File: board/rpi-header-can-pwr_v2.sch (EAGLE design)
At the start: 41 parts, among them U1 MCP2515, X1 RJ45-8L21-S, X2 RASPI_BOARD_B+#_E3

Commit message: add board temp sensor add battery voltage sensor
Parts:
- added C13, C15: 100n, rcl:C-EUC0603
- added C14: 1u, rcl:C-EUC0603
- added R7: 0, resistor:R-EU_R0603
- added R8, R9: 4.7K, resistor:R-EU_R0603
- added U2: ADS1015, SparkFun-IC-Conversion:ADS1015
- added U3: BME280, SparkFun-Sensors:BME280
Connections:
- new net ADC_ALERT: R7.1, X2.GPIO21
- new net ADC_INPUT_1: U2.AIN0
- new net I2C_SCL: R9.2, U2.SCL, U3.SCK/SCL, X2.SCL
- new net I2C_SDA: R8.2, U2.SDA, U3.SDI/SDA, X2.SDA
- new net N$9: R7.2, U2.ALERT/RDY
- net +3V3: now also C13.1, C14.1, C15.1, R8.1, R9.1, U2.VDD, U3.!CS, U3.VDD, U3.VDDIO
- net GND: now also C13.2, C14.2, C15.2, U2.ADDR, U2.VSS, U3.GND, U3.SDO/ADR

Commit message: ADC ALERT requires pull up
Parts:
- added R10: 4.7K, resistor:R-EU_R0603
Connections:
- net +3V3: now also R10.2
- net N$9: now also R10.1
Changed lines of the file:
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@@
 <part name="C14" library="rcl" deviceset="C-EU" device="C0603" value="1u"/>
 <part name="C15" library="rcl" deviceset="C-EU" device="C0603" value="100n"/>
+<part name="R10" library="resistor" deviceset="R-EU_" device="R0603" value="4.7K"/>
+<part name="+3V10" library="supply1" deviceset="+3V3" device=""/>
 </parts>
 <sheets>
@@
 <instance part="GND22" gate="1" x="142.24" y="10.16" rot="R90"/>
 <instance part="+3V9" gate="G$1" x="142.24" y="22.86" rot="R270"/>
+<instance part="R10" gate="G$1" x="35.56" y="-12.7" rot="R90"/>
+<instance part="+3V10" gate="G$1" x="35.56" y="0"/>
 </instances>
 <busses>
@@
 <wire x1="139.7" y1="22.86" x2="134.62" y2="22.86" width="0.1524" layer="91"/>
 </segment>
+<segment>
+<pinref part="R10" gate="G$1" pin="2"/>
+<pinref part="+3V10" gate="G$1" pin="+3V3"/>
+<wire x1="35.56" y1="-2.54" x2="35.56" y2="-7.62" width="0.1524" layer="91"/>
+</segment>
 </net>
 <net name="CAN_H" class="0">
@@
 <pinref part="U2" gate="G$1" pin="ALERT/RDY"/>
 <pinref part="R7" gate="G$1" pin="2"/>
-<wire x1="40.64" y1="-22.86" x2="33.02" y2="-22.86" width="0.1524" layer="91"/>
-</segment>
-</net>
+<wire x1="40.64" y1="-22.86" x2="35.56" y2="-22.86" width="0.1524" layer="91"/>
+<pinref part="R10" gate="G$1" pin="1"/>
+<wire x1="35.56" y1="-22.86" x2="33.02" y2="-22.86" width="0.1524" layer="91"/>
+<wire x1="35.56" y1="-17.78" x2="35.56" y2="-22.86" width="0.1524" layer="91"/>
+<junction x="35.56" y="-22.86"/>
+</segment>
+</net>

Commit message: add voltage divider and gpio protection to battery voltage sensor
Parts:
- added C29: 10nF, eagle-ltspice:CC0603
- added D7: BAS70-04, diode:BAS70-04
- added R20: 68k, rcl:R-EU_R0603
- added R21: 20k, rcl:R-EU_R0603
- added R22: 1k, rcl:R-EU_R0603
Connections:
- new net 12V_REFERENCE4: D7.C1A2, R20.2, R21.2, R22.1
- net +12V: now also R20.1
- net +3V3: now also D7.C2
- net ADC_INPUT_1: now also C29.2, R22.2
- net GND: now also C29.1, D7.A1, R21.1
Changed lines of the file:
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@@
 <part name="GND19" library="supply1" deviceset="GND" device=""/>
 <part name="R7" library="resistor" deviceset="R-EU_" device="R0603" value="0"/>
-<part name="P+8" library="supply1" deviceset="+12V" device=""/>
 <part name="R8" library="resistor" deviceset="R-EU_" device="R0603" value="4.7K"/>
 <part name="R9" library="resistor" deviceset="R-EU_" device="R0603" value="4.7K"/>
@@
 <part name="R10" library="resistor" deviceset="R-EU_" device="R0603" value="4.7K"/>
 <part name="+3V10" library="supply1" deviceset="+3V3" device=""/>
+<part name="R20" library="rcl" deviceset="R-EU_" device="R0603" value="68k"/>
+<part name="R21" library="rcl" deviceset="R-EU_" device="R0603" value="20k"/>
+<part name="D7" library="diode" deviceset="BAS70-04" device=""/>
+<part name="+3V16" library="supply1" deviceset="+3V3" device=""/>
+<part name="GND48" library="supply1" deviceset="GND" device=""/>
+<part name="C29" library="eagle-ltspice" deviceset="C" device="C0603" value="10nF"/>
+<part name="GND49" library="supply1" deviceset="GND" device=""/>
+<part name="GND50" library="supply1" deviceset="GND" device=""/>
+<part name="R22" library="rcl" deviceset="R-EU_" device="R0603" value="1k"/>
+<part name="P+10" library="supply1" deviceset="+12V" device=""/>
 </parts>
 <sheets>
@@
 <instance part="GND19" gate="1" x="38.1" y="-30.48" rot="R90"/>
 <instance part="R7" gate="G$1" x="45.72" y="-22.86" rot="R180"/>
-<instance part="P+8" gate="1" x="-35.56" y="-68.58" rot="R90"/>
 <instance part="R8" gate="G$1" x="27.94" y="-60.96" rot="R180"/>
 <instance part="R9" gate="G$1" x="27.94" y="-68.58" rot="R180"/>
@@
 <instance part="R10" gate="G$1" x="35.56" y="-12.7" rot="R90"/>
 <instance part="+3V10" gate="G$1" x="35.56" y="0"/>
+<instance part="R20" gate="G$1" x="-76.2" y="-88.9"/>
+<instance part="R21" gate="G$1" x="-55.88" y="-93.98"/>
+<instance part="D7" gate="G$1" x="-50.8" y="-81.28" rot="R180"/>
+<instance part="+3V16" gate="G$1" x="-63.5" y="-81.28" rot="R90"/>
+<instance part="GND48" gate="1" x="-40.64" y="-81.28" rot="R90"/>
+<instance part="C29" gate="G$1" x="-35.56" y="-83.82"/>
+<instance part="GND49" gate="1" x="-35.56" y="-78.74" rot="R180"/>
+<instance part="GND50" gate="1" x="-66.04" y="-93.98" rot="R270"/>
+<instance part="R22" gate="G$1" x="-43.18" y="-88.9"/>
+<instance part="P+10" gate="1" x="-88.9" y="-88.9" rot="R90"/>
 </instances>
 <busses>
@@
 <pinref part="GND22" gate="1" pin="GND"/>
 <wire x1="139.7" y1="10.16" x2="134.62" y2="10.16" width="0.1524" layer="91"/>
+</segment>
+<segment>
+<pinref part="C29" gate="G$1" pin="1"/>
+<pinref part="GND49" gate="1" pin="GND"/>
+</segment>
+<segment>
+<pinref part="D7" gate="G$1" pin="A1"/>
+<pinref part="GND48" gate="1" pin="GND"/>
+<wire x1="-45.72" y1="-81.28" x2="-43.18" y2="-81.28" width="0.1524" layer="91"/>
+</segment>
+<segment>
+<pinref part="R21" gate="G$1" pin="1"/>
+<wire x1="-63.5" y1="-93.98" x2="-60.96" y2="-93.98" width="0.1524" layer="91"/>
+<pinref part="GND50" gate="1" pin="GND"/>
 </segment>
 </net>
@@
 <wire x1="35.56" y1="-2.54" x2="35.56" y2="-7.62" width="0.1524" layer="91"/>
 </segment>
+<segment>
+<pinref part="+3V16" gate="G$1" pin="+3V3"/>
+<pinref part="D7" gate="G$1" pin="C2"/>
+<wire x1="-60.96" y1="-81.28" x2="-55.88" y2="-81.28" width="0.1524" layer="91"/>
+</segment>
 </net>
 <net name="CAN_H" class="0">
@@
 </segment>
 <segment>
-<pinref part="P+8" gate="1" pin="+12V"/>
-<wire x1="-33.02" y1="-68.58" x2="-25.4" y2="-68.58" width="0.1524" layer="91"/>
-<label x="-25.4" y="-68.58" size="1.778" layer="95" xref="yes"/>
+<wire x1="-35.56" y1="-88.9" x2="-27.94" y2="-88.9" width="0.1524" layer="91"/>
+<pinref part="C29" gate="G$1" pin="2"/>
+<label x="-27.94" y="-88.9" size="1.778" layer="95" xref="yes"/>
+<pinref part="R22" gate="G$1" pin="2"/>
+<wire x1="-38.1" y1="-88.9" x2="-35.56" y2="-88.9" width="0.1524" layer="91"/>
+<junction x="-35.56" y="-88.9"/>
 </segment>
 </net>
@@
 </segment>
 </net>
+<net name="12V_REFERENCE4" class="0">
+<segment>
+<pinref part="R20" gate="G$1" pin="2"/>
+<wire x1="-71.12" y1="-88.9" x2="-50.8" y2="-88.9" width="0.1524" layer="91"/>
+<junction x="-50.8" y="-88.9"/>
+<pinref part="R21" gate="G$1" pin="2"/>
+<wire x1="-50.8" y1="-88.9" x2="-50.8" y2="-93.98" width="0.1524" layer="91"/>
+<pinref part="D7" gate="G$1" pin="C1A2"/>
+<wire x1="-50.8" y1="-83.82" x2="-50.8" y2="-88.9" width="0.1524" layer="91"/>
+<pinref part="R22" gate="G$1" pin="1"/>
+<wire x1="-48.26" y1="-88.9" x2="-50.8" y2="-88.9" width="0.1524" layer="91"/>
+</segment>
+</net>
+<net name="+12V" class="0">
+<segment>
+<pinref part="R20" gate="G$1" pin="1"/>
+<pinref part="P+10" gate="1" pin="+12V"/>
+<wire x1="-86.36" y1="-88.9" x2="-81.28" y2="-88.9" width="0.1524" layer="91"/>
+</segment>
+</net>

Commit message: change to microfit from rj45
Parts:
- removed GND84: (no value), SparkFun-Connectors:CONN_023.5MM
- removed J1: (no value), SparkFun-Connectors:CONN_025MM
- removed JP1: (no value), jumper:JP1Q
- removed R25: 10k, rcl:R-EU_R0603
- removed R5: 120, rcl:R-EU_R0603
- removed X1: RJ45-8L21-S, con-tycoelectronics:RJ45-8L21-S
- added JP2: (no value), jumper:JP1Q
- added R11: 120, rcl:R-EU_R0603
- added X3, X4: (no value), con-molex-micro-fit-3_0:HEADER_POS8_43045-0812
- added X5: JST-XH-02-PIN-LONG-PAD, Rembrandt Electronics - JST XH Connectors v1-0:JST-XH-02-PIN-LONG-PAD
- added X6: 5566-2, con-molex:5566-2
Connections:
- removed net N$20: R25.1, X1.S@1, X1.S@2
- removed net N$5: F3.1, JP1.1
- removed net RJ45_12V: JP1.2, X1.4, X1.5, X1.6
- new net CAN_PWR: F3.1, X3.2, X3.3, X3.4, X4.2, X4.3, X4.4
- new net N$12: JP2.2, R11.1
- net CAN_H: now also R11.2, X3.1, X4.1; no longer R5.2, X1.1
- net CAN_L: now also JP2.1, X3.5, X4.5; no longer R5.1, X1.2
- net GND: now also X3.6, X3.7, X3.8, X4.6, X4.7, X4.8, X6-2.S; no longer J1.1, R25.2, X1.3, X1.7, X1.8
- net N$10: now also X5-2.S; no longer GND84.2
- net N$11: now also X5-1.S; no longer GND84.1
- net PRE_FUSE_12V: now also X6-1.S; no longer J1.2
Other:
- moved on the sheet: F1

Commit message: add lora support
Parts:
- removed X5: JST-XH-02-PIN-LONG-PAD, Rembrandt Electronics - JST XH Connectors v1-0:JST-XH-02-PIN-LONG-PAD
- added C16: 0.1uF, microbuilder:CAP_CERAMIC0603_NO
- added C17: 10uF, microbuilder:CAP_CERAMIC0805-NOOUTLINE
- added J1: U.FL, SparkFun-Connectors:U.FL
- added J2: (no value), SparkFun-Connectors:CONN_023.5MM
- added R14, R15, R17: 10k, rcl:R-EU_R0603
- added U4: RFM69HCW, microbuilder:RFM69HCW_SMT
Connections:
- new net LORA_CS: R14.2, U4.NSS, X2.SPI_CE1
- new net LORA_DIO0: U4.DIO0, X2.GPIO22
- new net LORA_DIO1: U4.DIO1, X2.GPIO23
- new net LORA_DIO2: U4.DIO2, X2.GPIO24
- new net LORA_RST: R17.2, U4.RESET, X2.GPIO25
- new net N$5: J1.SIGNAL, U4.ANT
- net +3V3: now also C16.1, C17.1, R14.1, R15.1, R17.1, U4.VDD
- net CAN_CS: now also R15.2
- net GND: now also C16.2, C17.2, J1.GND@0, J1.GND@1, U4.GND@1, U4.GND@2, U4.GND@3
- net MISO: now also U4.MISO
- net MOSI: now also U4.MOSI
- net N$10: now also J2.2; no longer X5-2.S
- net N$11: now also J2.1; no longer X5-1.S
- net SCK: now also U4.SCK

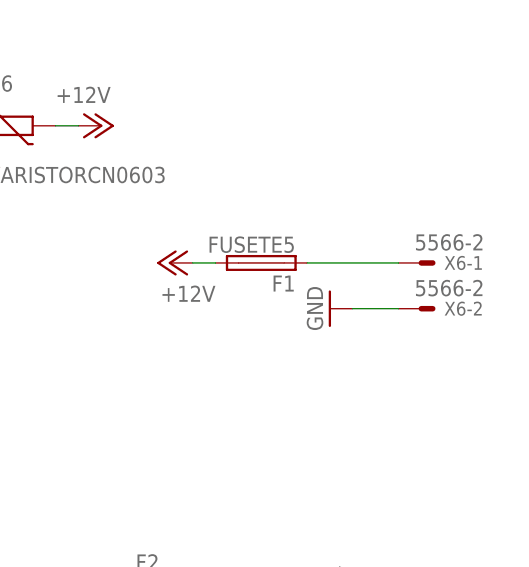
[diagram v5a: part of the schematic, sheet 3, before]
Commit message: change power connector to 5mm screw terminal
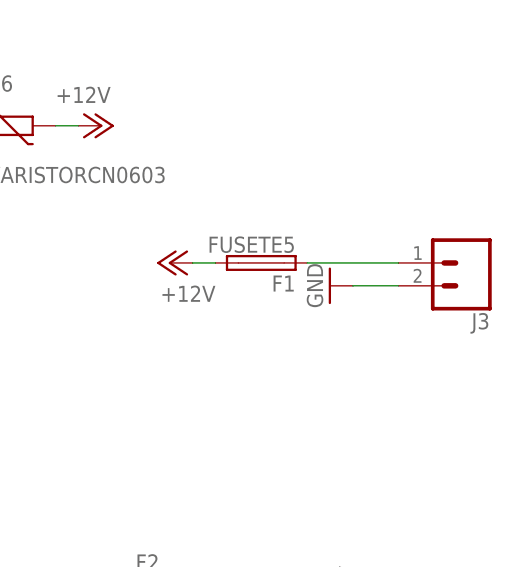
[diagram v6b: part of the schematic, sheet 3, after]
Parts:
- removed X6: 5566-2, con-molex:5566-2
- added J3: (no value), SparkFun-Connectors:CONN_025MM
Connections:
- net GND: now also J3.2; no longer X6-2.S
- net PRE_FUSE_12V: now also J3.1; no longer X6-1.S
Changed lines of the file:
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@@
 <part name="R11" library="rcl" deviceset="R-EU_" device="R0603" value="120"/>
 <part name="JP2" library="jumper" deviceset="JP1Q" device=""/>
-<part name="X6" library="con-molex" deviceset="5566-2" device=""/>
 <part name="GND17" library="supply1" deviceset="GND" device=""/>
 <part name="U4" library="microbuilder" deviceset="RFM69HCW" device="_SMT" value="RFM69HCW"/>
@@
 <part name="+3V15" library="supply1" deviceset="+3V3" device=""/>
 <part name="J2" library="SparkFun-Connectors" deviceset="CONN_02" device="3.5MM"/>
+<part name="J3" library="SparkFun-Connectors" deviceset="CONN_02" device="5MM"/>
 </parts>
 <sheets>
@@
 <instance part="P+5" gate="1" x="180.34" y="93.98" rot="R270"/>
 <instance part="GND20" gate="1" x="160.02" y="93.98" rot="R270"/>
-<instance part="X6" gate="-1" x="215.9" y="78.74"/>
-<instance part="X6" gate="-2" x="215.9" y="73.66"/>
-<instance part="GND17" gate="1" x="205.74" y="73.66" rot="R270"/>
+<instance part="GND17" gate="1" x="205.74" y="76.2" rot="R270"/>
+<instance part="J3" gate="G$1" x="220.98" y="78.74" rot="R180"/>
 </instances>
 <busses>
@@
 </segment>
 <segment>
-<pinref part="X6" gate="-2" pin="S"/>
 <pinref part="GND17" gate="1" pin="GND"/>
-<wire x1="208.28" y1="73.66" x2="213.36" y2="73.66" width="0.1524" layer="91"/>
+<wire x1="208.28" y1="76.2" x2="213.36" y2="76.2" width="0.1524" layer="91"/>
+<pinref part="J3" gate="G$1" pin="2"/>
 </segment>
 </net>
@@
 <segment>
 <pinref part="F1" gate="G$1" pin="1"/>
-<pinref part="X6" gate="-1" pin="S"/>
 <wire x1="203.2" y1="78.74" x2="213.36" y2="78.74" width="0.1524" layer="91"/>
-</segment>
-</net>
+<pinref part="J3" gate="G$1" pin="1"/>
+</segment>
+</net>

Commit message: fan support
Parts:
- removed JP2: (no value), jumper:JP1Q
- removed X3: (no value), con-molex-micro-fit-3_0:HEADER_POS8_43045-0812
- added F4: 1210L010, polyfuse-smd_10:1210L010
- added J7: (no value), SparkFun-Connectors:CONN_023.5MM
- added R5: 500, rcl:R-EU_R0603
- added T2: (no value), zetex:NPNSOT23
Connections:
- new net FAN_PWM: R5.1, X2.GPIO18
- new net N$13: F4.1, J7.1
- new net N$14: J7.2, T2.C
- net CAN_H: no longer X3.1
- net CAN_L: now also R11.1; no longer JP2.1, X3.5
- net CAN_PWR: no longer X3.2, X3.3, X3.4
- net GND: now also T2.E; no longer X3.6, X3.7, X3.8
- net N$12: now also R5.2, T2.B; no longer JP2.2, R11.1
- net PRE_FUSE_12V: now also F4.2
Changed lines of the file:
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@@
 <part name="P+10" library="supply1" deviceset="+12V" device=""/>
 <part name="GND23" library="supply1" deviceset="GND" device=""/>
-<part name="GND24" library="supply1" deviceset="GND" device=""/>
-<part name="GND25" library="supply1" deviceset="GND" device=""/>
 <part name="GND26" library="supply1" deviceset="GND" device=""/>
-<part name="X3" library="con-molex-micro-fit-3_0" deviceset="HEADER_POS8_?" device="43045-0812"/>
 <part name="X4" library="con-molex-micro-fit-3_0" deviceset="HEADER_POS8_?" device="43045-0812"/>
-<part name="GND27" library="supply1" deviceset="GND" device=""/>
 <part name="GND29" library="supply1" deviceset="GND" device=""/>
 <part name="R11" library="rcl" deviceset="R-EU_" device="R0603" value="120"/>
-<part name="JP2" library="jumper" deviceset="JP1Q" device=""/>
 <part name="GND17" library="supply1" deviceset="GND" device=""/>
 <part name="U4" library="microbuilder" deviceset="RFM69HCW" device="_SMT" value="RFM69HCW"/>
@@
 <part name="J2" library="SparkFun-Connectors" deviceset="CONN_02" device="3.5MM"/>
 <part name="J3" library="SparkFun-Connectors" deviceset="CONN_02" device="5MM"/>
+<part name="F4" library="polyfuse-smd_10" deviceset="?" device="1210L" technology="010"/>
+<part name="T2" library="zetex" deviceset="NPNSOT23" device=""/>
+<part name="R5" library="rcl" deviceset="R-EU_" device="R0603" value="500"/>
+<part name="J7" library="SparkFun-Connectors" deviceset="CONN_02" device="3.5MM"/>
+<part name="GND18" library="supply1" deviceset="GND" device=""/>
 </parts>
 <sheets>
@@
 <instance part="P+10" gate="1" x="-88.9" y="-88.9" rot="R90"/>
 <instance part="GND23" gate="1" x="-119.38" y="-20.32"/>
-<instance part="GND24" gate="1" x="-83.82" y="-20.32"/>
-<instance part="GND25" gate="1" x="-81.28" y="-20.32"/>
 <instance part="GND26" gate="1" x="-116.84" y="-20.32"/>
-<instance part="X3" gate="G$1" x="-88.9" y="-7.62" rot="R90"/>
 <instance part="X4" gate="G$1" x="-124.46" y="-7.62" rot="R90"/>
-<instance part="GND27" gate="1" x="-86.36" y="-20.32"/>
 <instance part="GND29" gate="1" x="-121.92" y="-20.32"/>
 <instance part="R11" gate="G$1" x="-76.2" y="0" rot="R180"/>
-<instance part="JP2" gate="A" x="-60.96" y="0" rot="R90"/>
 </instances>
 <busses>
@@
 </segment>
 <segment>
-<wire x1="-83.82" y1="-12.7" x2="-83.82" y2="-17.78" width="0.1524" layer="91"/>
-<pinref part="GND24" gate="1" pin="GND"/>
-<pinref part="X3" gate="G$1" pin="7"/>
-</segment>
-<segment>
-<wire x1="-81.28" y1="-12.7" x2="-81.28" y2="-17.78" width="0.1524" layer="91"/>
-<pinref part="GND25" gate="1" pin="GND"/>
-<pinref part="X3" gate="G$1" pin="8"/>
-</segment>
-<segment>
 <wire x1="-116.84" y1="-12.7" x2="-116.84" y2="-17.78" width="0.1524" layer="91"/>
 <pinref part="GND26" gate="1" pin="GND"/>
 <pinref part="X4" gate="G$1" pin="8"/>
-</segment>
-<segment>
-<pinref part="X3" gate="G$1" pin="6"/>
-<wire x1="-86.36" y1="-12.7" x2="-86.36" y2="-17.78" width="0.1524" layer="91"/>
-<pinref part="GND27" gate="1" pin="GND"/>
 </segment>
 <segment>
@@
 </segment>
 <segment>
-<wire x1="-99.06" y1="-12.7" x2="-99.06" y2="-17.78" width="0.1524" layer="91"/>
-<label x="-99.06" y="-17.78" size="1.778" layer="95" rot="R270" xref="yes"/>
-<pinref part="X3" gate="G$1" pin="1"/>
-</segment>
-<segment>
 <pinref part="R11" gate="G$1" pin="2"/>
 <wire x1="-81.28" y1="0" x2="-86.36" y2="0" width="0.1524" layer="91"/>
@@
 </segment>
 <segment>
-<pinref part="X3" gate="G$1" pin="5"/>
-<wire x1="-88.9" y1="-12.7" x2="-88.9" y2="-17.78" width="0.1524" layer="91"/>
-<label x="-88.9" y="-17.78" size="1.778" layer="95" rot="R270" xref="yes"/>
-</segment>
-<segment>
-<pinref part="JP2" gate="A" pin="1"/>
-<wire x1="-53.34" y1="0" x2="-48.26" y2="0" width="0.1524" layer="91"/>
-<label x="-48.26" y="0" size="1.778" layer="95" xref="yes"/>
+<pinref part="R11" gate="G$1" pin="1"/>
+<wire x1="-66.04" y1="0" x2="-71.12" y2="0" width="0.1524" layer="91"/>
+<label x="-66.04" y="0" size="1.778" layer="95" xref="yes"/>
 </segment>
 </net>
@@
 </segment>
 <segment>
-<pinref part="X3" gate="G$1" pin="2"/>
-<wire x1="-96.52" y1="-12.7" x2="-96.52" y2="-25.4" width="0.1524" layer="91"/>
-<label x="-96.52" y="-25.4" size="1.778" layer="95" rot="R270" xref="yes"/>
-</segment>
-<segment>
-<pinref part="X3" gate="G$1" pin="3"/>
-<wire x1="-93.98" y1="-12.7" x2="-93.98" y2="-25.4" width="0.1524" layer="91"/>
-<label x="-93.98" y="-25.4" size="1.778" layer="95" rot="R270" xref="yes"/>
-</segment>
-<segment>
-<wire x1="-91.44" y1="-12.7" x2="-91.44" y2="-25.4" width="0.1524" layer="91"/>
-<label x="-91.44" y="-25.4" size="1.778" layer="95" rot="R270" xref="yes"/>
-<pinref part="X3" gate="G$1" pin="4"/>
-</segment>
-<segment>
 <label x="-25.4" y="12.7" size="1.778" layer="95" rot="R180" xref="yes"/>
 <pinref part="F3" gate="G$1" pin="1"/>
 <wire x1="-25.4" y1="12.7" x2="-15.24" y2="12.7" width="0.1524" layer="91"/>
-</segment>
-</net>
-<net name="N$12" class="0">
-<segment>
-<pinref part="R11" gate="G$1" pin="1"/>
-<pinref part="JP2" gate="A" pin="2"/>
-<wire x1="-68.58" y1="0" x2="-71.12" y2="0" width="0.1524" layer="91"/>
 </segment>
 </net>
@@
 </segment>
 </net>
+<net name="FAN_PWM" class="0">
+<segment>
+<pinref part="X2" gate="G$1" pin="GPIO18"/>
+<wire x1="-93.98" y1="35.56" x2="-99.06" y2="35.56" width="0.1524" layer="91"/>
+<label x="-99.06" y="35.56" size="1.778" layer="95" rot="R270" xref="yes"/>
+</segment>
+</net>
 </nets>
 </sheet>
@@
 </segment>
 </net>
+</nets>
+</sheet>
+<sheet>
+<plain>
+</plain>
+<instances>
+<instance part="F4" gate="G$1" x="43.18" y="71.12"/>
+<instance part="T2" gate="A" x="22.86" y="38.1"/>
+<instance part="R5" gate="G$1" x="10.16" y="38.1"/>
+<instance part="J7" gate="G$1" x="58.42" y="71.12" rot="R180"/>
+<instance part="GND18" gate="1" x="25.4" y="25.4"/>
+</instances>
+<busses>
+</busses>
+<nets>
+<net name="N$12" class="0">
+<segment>
+<pinref part="T2" gate="A" pin="B"/>
+<pinref part="R5" gate="G$1" pin="2"/>
+<wire x1="15.24" y1="38.1" x2="20.32" y2="38.1" width="0.1524" layer="91"/>
+</segment>
+</net>
+<net name="FAN_PWM" class="0">
+<segment>
+<pinref part="R5" gate="G$1" pin="1"/>
+<wire x1="5.08" y1="38.1" x2="-5.08" y2="38.1" width="0.1524" layer="91"/>
+<label x="-5.08" y="38.1" size="1.778" layer="95" rot="R180" xref="yes"/>
+</segment>
+</net>
+<net name="GND" class="0">
+<segment>
+<pinref part="T2" gate="A" pin="E"/>
+<wire x1="25.4" y1="33.02" x2="25.4" y2="27.94" width="0.1524" layer="91"/>
+<pinref part="GND18" gate="1" pin="GND"/>
+</segment>
+</net>
+<net name="N$13" class="0">
+<segment>
+<pinref part="J7" gate="G$1" pin="1"/>
+<pinref part="F4" gate="G$1" pin="1"/>
+<wire x1="48.26" y1="71.12" x2="50.8" y2="71.12" width="0.1524" layer="91"/>
+</segment>
+</net>
+<net name="PRE_FUSE_12V" class="0">
+<segment>
+<pinref part="F4" gate="G$1" pin="2"/>
+<wire x1="38.1" y1="71.12" x2="35.56" y2="71.12" width="0.1524" layer="91"/>
+<label x="35.56" y="71.12" size="1.778" layer="95" rot="R180" xref="yes"/>
+</segment>
+</net>
+<net name="N$14" class="0">
+<segment>
+<pinref part="T2" gate="A" pin="C"/>
+<pinref part="J7" gate="G$1" pin="2"/>
+<wire x1="25.4" y1="43.18" x2="25.4" y2="68.58" width="0.1524" layer="91"/>
+<wire x1="25.4" y1="68.58" x2="50.8" y2="68.58" width="0.1524" layer="91"/>
+</segment>
+</net>
